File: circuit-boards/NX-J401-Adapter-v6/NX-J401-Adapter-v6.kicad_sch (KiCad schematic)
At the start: 28 parts, among them J10 NX CONTROL & UART, J2 POWER, J3 USB1, J4 Terminal, J5 CAN1, J6 Terminal, J7 15V, Q10 CSD19534Q5A, Q9 CSD19534Q5A, SW1 RECOVERY, SW2 RESET, U2 LM74700QDBVRQ1, U6 LM74700QDBVRQ1

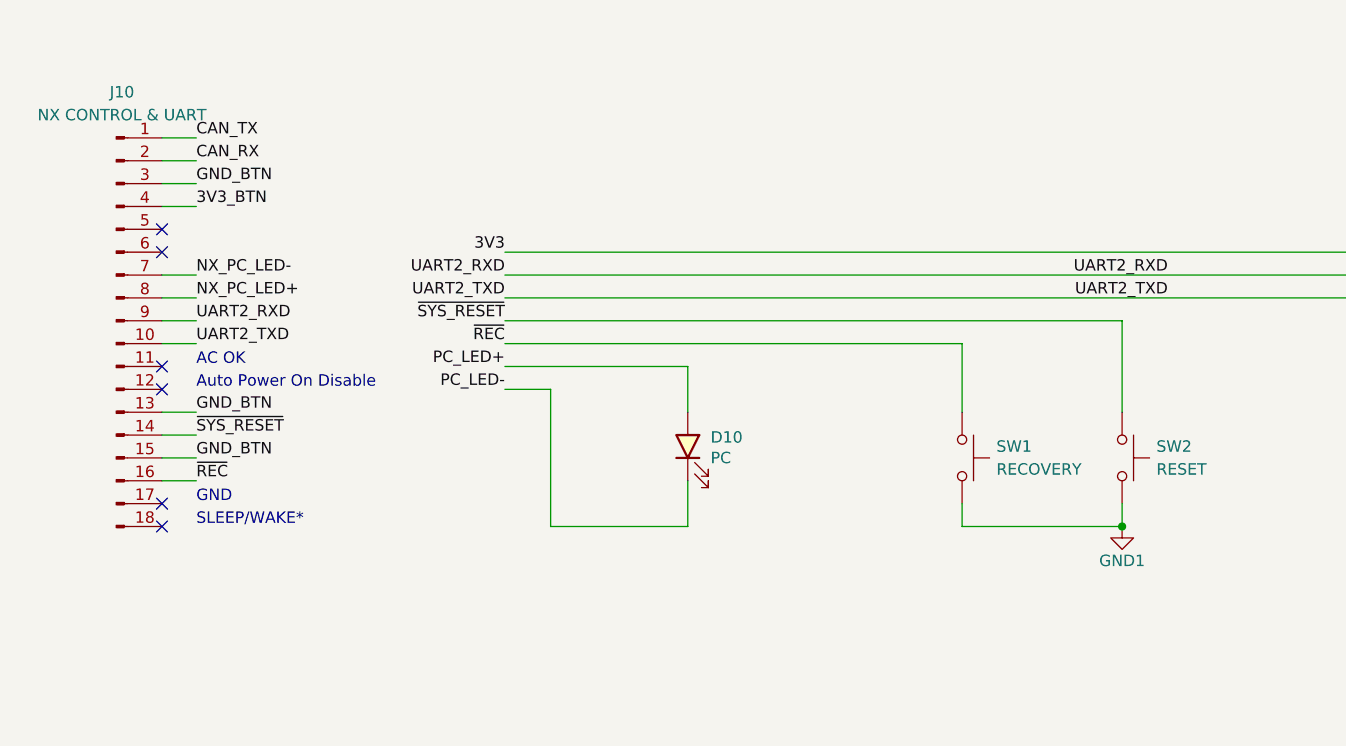
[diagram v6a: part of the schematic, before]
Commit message: Initial fully routed PCB
Signed-off-by: Scott Berman <sgberman1@gmail.com>
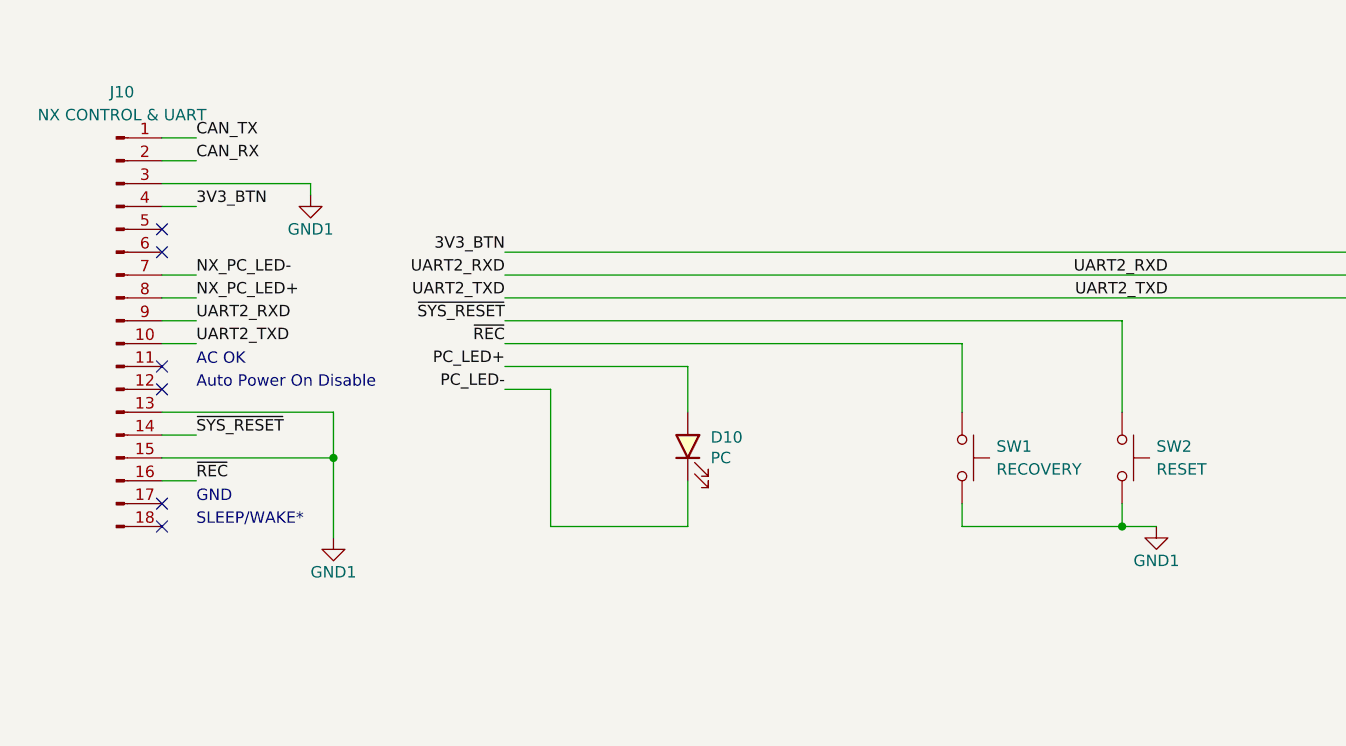
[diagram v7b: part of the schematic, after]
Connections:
- net GND_BTN is gone; now on net GND1: J10.13 (Pin_13), J10.15 (Pin_15), J10.3 (Pin_3)
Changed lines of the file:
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@@
 	)
 	(junction
+		(at 63.5 203.2)
+		(diameter 0)
+		(color 0 0 0 0)
+	)
+	(junction
 		(at 124.46 45.72)
 		(diameter 0)
@@
 	(wire
 		(pts
+			(xy 60.96 172.72) (xy 44.45 172.72)
+		)
+		(stroke
+			(width 0)
+			(type default)
+		)
+	)
+	(wire
+		(pts
 			(xy 92.71 63.5) (xy 92.71 45.72)
 		)
@@
 	(wire
 		(pts
-			(xy 48.26 198.12) (xy 44.45 198.12)
+			(xy 44.45 198.12) (xy 63.5 198.12)
 		)
 		(stroke
@@
 	(wire
 		(pts
+			(xy 63.5 198.12) (xy 63.5 203.2)
+		)
+		(stroke
+			(width 0)
+			(type default)
+		)
+	)
+	(wire
+		(pts
 			(xy 104.14 45.72) (xy 118.11 45.72)
 		)
@@
 	(wire
 		(pts
+			(xy 63.5 203.2) (xy 63.5 212.09)
+		)
+		(stroke
+			(width 0)
+			(type default)
+		)
+	)
+	(wire
+		(pts
 			(xy 48.26 205.74) (xy 44.45 205.74)
 		)
@@
 	(wire
 		(pts
+			(xy 60.96 173.99) (xy 60.96 172.72)
+		)
+		(stroke
+			(width 0)
+			(type default)
+		)
+	)
+	(wire
+		(pts
 			(xy 161.29 45.72) (xy 161.29 59.69)
 		)
@@
 	(wire
 		(pts
+			(xy 154.94 210.82) (xy 151.13 210.82)
+		)
+		(stroke
+			(width 0)
+			(type default)
+		)
+	)
+	(wire
+		(pts
 			(xy 143.51 81.28) (xy 161.29 81.28)
 		)
@@
 	(wire
 		(pts
-			(xy 48.26 203.2) (xy 44.45 203.2)
+			(xy 44.45 203.2) (xy 63.5 203.2)
 		)
 		(stroke
@@
 	(wire
 		(pts
-			(xy 48.26 172.72) (xy 44.45 172.72)
-		)
-		(stroke
-			(width 0)
-			(type default)
-		)
-	)
-	(wire
-		(pts
 			(xy 48.26 190.5) (xy 44.45 190.5)
 		)
@@
 		)
 	)
-	(label "GND_BTN"
-		(at 48.26 203.2 0)
-		(effects
-			(font
-				(size 1.27 1.27)
-			)
-			(justify left bottom)
-		)
-	)
 	(label "V_OUT_RTN"
 		(at 342.9 71.12 180)
@@
 		)
 	)
-	(label "GND_BTN"
-		(at 48.26 172.72 0)
+	(label "3V3_BTN"
+		(at 82.55 180.34 180)
 		(effects
 			(font
 				(size 1.27 1.27)
 			)
-			(justify left bottom)
+			(justify right bottom)
 		)
 	)
@@
 		)
 	)
-	(label "GND_BTN"
-		(at 48.26 198.12 0)
-		(effects
-			(font
-				(size 1.27 1.27)
-			)
-			(justify left bottom)
-		)
-	)
-	(label "3V3"
-		(at 82.55 180.34 180)
-		(effects
-			(font
-				(size 1.27 1.27)
-			)
-			(justify right bottom)
-		)
-	)
 	(label "CAN_RX"
 		(at 48.26 170.18 0)
@@
 	)
 	(symbol
+		(lib_id "power:GND")
+		(at 60.96 173.99 0)
+		(mirror y)
+		(unit 1)
+		(body_style 1)
+		(exclude_from_sim no)
+		(in_bom yes)
+		(on_board yes)
+		(in_pos_files yes)
+		(dnp no)
+		(property "Reference" "#PWR033"
+			(at 60.96 180.34 0)
+			(hide yes)
+			(show_name no)
+			(do_not_autoplace no)
+			(effects
+				(font
+					(size 1.27 1.27)
+				)
+			)
+		)
+		(property "Value" "GND1"
+			(at 60.96 177.8 0)
+			(show_name no)
+			(do_not_autoplace no)
+			(effects
+				(font
+					(size 1.27 1.27)
+				)
+			)
+		)
+		(property "Footprint" ""
+			(at 60.96 173.99 0)
+			(hide yes)
+			(show_name no)
+			(do_not_autoplace no)
+			(effects
+				(font
+					(size 1.27 1.27)
+				)
+			)
+		)
+		(property "Datasheet" ""
+			(at 60.96 173.99 0)
+			(hide yes)
+			(show_name no)
+			(do_not_autoplace no)
+			(effects
+				(font
+					(size 1.27 1.27)
+				)
+			)
+		)
+		(property "Description" ""
+			(at 60.96 173.99 0)
+			(hide yes)
+			(show_name no)
+			(do_not_autoplace no)
+			(effects
+				(font
+					(size 1.27 1.27)
+				)
+			)
+		)
+		(pin "1"
+		)
+		(instances
+			(project "NX-J401-Adapter-v6"
+				(path "/3c9fa76f-2b37-4666-8575-58caa65def04"
+					(reference "#PWR033")
+					(unit 1)
+				)
+			)
+		)
+	)
+	(symbol
+		(lib_id "power:GND")
+		(at 154.94 210.82 0)
+		(mirror y)
+		(unit 1)
+		(body_style 1)
+		(exclude_from_sim no)
+		(in_bom yes)
+		(on_board yes)
+		(in_pos_files yes)
+		(dnp no)
+		(property "Reference" "#PWR032"
+			(at 154.94 217.17 0)
+			(hide yes)
+			(show_name no)
+			(do_not_autoplace no)
+			(effects
+				(font
+					(size 1.27 1.27)
+				)
+			)
+		)
+		(property "Value" "GND1"
+			(at 154.94 214.63 0)
+			(show_name no)
+			(do_not_autoplace no)
+			(effects
+				(font
+					(size 1.27 1.27)
+				)
+			)
+		)
+		(property "Footprint" ""
+			(at 154.94 210.82 0)
+			(hide yes)
+			(show_name no)
+			(do_not_autoplace no)
+			(effects
+				(font
+					(size 1.27 1.27)
+				)
+			)
+		)
+		(property "Datasheet" ""
+			(at 154.94 210.82 0)
+			(hide yes)
+			(show_name no)
+			(do_not_autoplace no)
+			(effects
+				(font
+					(size 1.27 1.27)
+				)
+			)
+		)
+		(property "Description" ""
+			(at 154.94 210.82 0)
+			(hide yes)
+			(show_name no)
+			(do_not_autoplace no)
+			(effects
+				(font
+					(size 1.27 1.27)
+				)
+			)
+		)
+		(pin "1"
+		)
+		(instances
+			(project "NX-J401-Adapter-v6"
+				(path "/3c9fa76f-2b37-4666-8575-58caa65def04"
+					(reference "#PWR032")
+					(unit 1)
+				)
+			)
+		)
+	)
+	(symbol
 		(lib_name "LED_1")
 		(lib_id "Device:LED")
@@
 	)
 	(symbol
-		(lib_id "power:GND")
-		(at 151.13 210.82 0)
-		(mirror y)
-		(unit 1)
-		(body_style 1)
-		(exclude_from_sim no)
-		(in_bom yes)
-		(on_board yes)
-		(in_pos_files yes)
-		(dnp no)
-		(property "Reference" "#PWR01"
-			(at 151.13 217.17 0)
-			(hide yes)
-			(show_name no)
-			(do_not_autoplace no)
-			(effects
-				(font
-					(size 1.27 1.27)
-				)
-			)
-		)
-		(property "Value" "GND1"
-			(at 151.13 214.63 0)
-			(show_name no)
-			(do_not_autoplace no)
-			(effects
-				(font
-					(size 1.27 1.27)
-				)
-			)
-		)
-		(property "Footprint" ""
-			(at 151.13 210.82 0)
-			(hide yes)
-			(show_name no)
-			(do_not_autoplace no)
-			(effects
-				(font
-					(size 1.27 1.27)
-				)
-			)
-		)
-		(property "Datasheet" ""
-			(at 151.13 210.82 0)
-			(hide yes)
-			(show_name no)
-			(do_not_autoplace no)
-			(effects
-				(font
-					(size 1.27 1.27)
-				)
-			)
-		)
-		(property "Description" ""
-			(at 151.13 210.82 0)
-			(hide yes)
-			(show_name no)
-			(do_not_autoplace no)
-			(effects
-				(font
-					(size 1.27 1.27)
-				)
-			)
-		)
-		(pin "1"
-		)
-		(instances
-			(project "NX-J401-Adapter-v6"
-				(path "/3c9fa76f-2b37-4666-8575-58caa65def04"
-					(reference "#PWR01")
-					(unit 1)
-				)
-			)
-		)
-	)
-	(symbol
 		(lib_id "Device:C_US")
 		(at 130.81 57.15 0)
@@
 					(unit 1)
 				)
+			)
+		)
+	)
+	(symbol
+		(lib_id "power:GND")
+		(at 63.5 212.09 0)
+		(mirror y)
+		(unit 1)
+		(body_style 1)
+		(exclude_from_sim no)
+		(in_bom yes)
+		(on_board yes)
+		(in_pos_files yes)
+		(dnp no)
+		(property "Reference" "#PWR034"
+			(at 63.5 218.44 0)
+			(hide yes)
+			(show_name no)
+			(do_not_autoplace no)
+			(effects
+				(font
+					(size 1.27 1.27)
+				)
+			)
+		)
+		(property "Value" "GND1"
+			(at 63.5 215.9 0)
+			(show_name no)
+			(do_not_autoplace no)
+			(effects
+				(font
+					(size 1.27 1.27)
+				)
+			)
+		)
+		(property "Footprint" ""
+			(at 63.5 212.09 0)
+			(hide yes)
+			(show_name no)
+			(do_not_autoplace no)
+			(effects
+				(font
+					(size 1.27 1.27)
+				)
+			)
+		)
+		(property "Datasheet" ""
+			(at 63.5 212.09 0)
+			(hide yes)
+			(show_name no)
+			(do_not_autoplace no)
+			(effects
+				(font
+					(size 1.27 1.27)
+				)
+			)
+		)
+		(property "Description" ""
+			(at 63.5 212.09 0)
+			(hide yes)
+			(show_name no)
+			(do_not_autoplace no)
+			(effects
+				(font
+					(size 1.27 1.27)
+				)
+			)
+		)
+		(pin "1"
+		)
+		(instances
+			(project "NX-J401-Adapter-v6"
+				(path "/3c9fa76f-2b37-4666-8575-58caa65def04"
+					(reference "#PWR034")
+					(unit 1)
+				)

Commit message: Initial complete routing
Signed-off-by: Scott Berman <sgberman1@gmail.com>
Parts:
- C10: renamed from C33; KiLib_Generator (none) -> SMD_2terminal_chip_molded
- C4: renamed from C39; KiLib_Generator (none) -> SMD_2terminal_chip_molded
- C40: renamed from C1; KiLib_Generator (none) -> SMD_2terminal_chip_molded
- C41: renamed from C35; KiLib_Generator (none) -> SMD_2terminal_chip_molded
- C42: renamed from C6; KiLib_Generator (none) -> SMD_2terminal_chip_molded
- C5: renamed from C34; KiLib_Generator (none) -> SMD_2terminal_chip_molded
- D6: renamed from D9; KiLib_Generator (none) -> SMD_2terminal_chip_molded
- D7: renamed from D10; KiLib_Generator (none) -> SMD_2terminal_chip_molded
- H1: KiLib_Generator (none) -> mounting_hardware/mounting_hole
- H2: renamed from H4; KiLib_Generator (none) -> mounting_hardware/mounting_hole
- H3: renamed from H2; KiLib_Generator (none) -> mounting_hardware/mounting_hole
- H4: renamed from H3; KiLib_Generator (none) -> mounting_hardware/mounting_hole
- J10: renamed from J2; KiLib_Generator (none) -> connector/Molex
- J5: renamed from J10; KiLib_Generator (none) -> connector/pin_header_socket
- J7: KiLib_Generator (none) -> connector/Molex
- R16: renamed from R18; KiLib_Generator (none) -> SMD_2terminal_chip_molded
- U2: renamed from U6; KiLib_Generator (none) -> package/gullwing
- U4: renamed from U2; KiLib_Generator (none) -> package/gullwing
- renumbered D2 to D3, J4 to J1, J6 to J2, J3 to J6, J5 to J9, Q10 to Q2, SW2 to SW1, SW1 to SW2
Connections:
- net PC_LED+ is gone; now on net NX_PC_LED+: D7.2 (A)
- net PC_LED- is gone; now on net NX_PC_LED-: D7.1 (K)
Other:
- moved on the sheet: D7
